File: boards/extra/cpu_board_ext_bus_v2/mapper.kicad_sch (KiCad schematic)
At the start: 3 parts, among them U2 74LS30, U7 74LS30, U8 ATF1502AS-7JX44

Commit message: Preparation for ordering with PCBWay.
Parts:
- U2, U7: MPN (none) -> 1-2199298-3; Manufacturer (none) -> TE Connectivity; Package (none) -> DIP-14
- U8: MPN (none) -> DS1032-44SDKT1A; Manufacturer (none) -> CONNFLY Elec; Package (none) -> Plugin-44P
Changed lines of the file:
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@@
       (effects (font (size 1.524 1.524)))
+    )
+    (property "Description" " 	44P PLCC Tin 1.27mm Plugin-44P IC / Transistor Socket ROHS " (at 182.245 66.675 0)
+      (effects (font (size 1.27 1.27)) hide)
+    )
+    (property "MPN" "DS1032-44SDKT1A" (at 182.245 66.675 0)
+      (effects (font (size 1.27 1.27)) hide)
+    )
+    (property "Manufacturer" " 	CONNFLY Elec " (at 182.245 66.675 0)
+      (effects (font (size 1.27 1.27)) hide)
+    )
+    (property "Package" " Plugin-44P" (at 182.245 66.675 0)
+      (effects (font (size 1.27 1.27)) hide)
     )
     (pin "3")
@@
       (effects (font (size 1.27 1.27)) hide)
     )
+    (property "Description" " 	Tin Phosphor bronze DIP-14 IC / Transistor Socket ROHS " (at 100.965 184.15 0)
+      (effects (font (size 1.27 1.27)) hide)
+    )
+    (property "MPN" "1-2199298-3" (at 100.965 184.15 0)
+      (effects (font (size 1.27 1.27)) hide)
+    )
+    (property "Manufacturer" "TE Connectivity " (at 100.965 184.15 0)
+      (effects (font (size 1.27 1.27)) hide)
+    )
+    (property "Package" "DIP-14" (at 100.965 184.15 0)
+      (effects (font (size 1.27 1.27)) hide)
+    )
     (pin "3")
     (pin "1")
@@
       (effects (font (size 1.27 1.27)) hide)
     )
+    (property "Description" " 	Tin Phosphor bronze DIP-14 IC / Transistor Socket ROHS " (at 116.205 54.61 0)
+      (effects (font (size 1.27 1.27)) hide)
+    )
+    (property "MPN" "1-2199298-3" (at 116.205 54.61 0)
+      (effects (font (size 1.27 1.27)) hide)
+    )
+    (property "Manufacturer" "TE Connectivity " (at 116.205 54.61 0)
+      (effects (font (size 1.27 1.27)) hide)
+    )
+    (property "Package" "DIP-14" (at 116.205 54.61 0)
+      (effects (font (size 1.27 1.27)) hide)
+    )

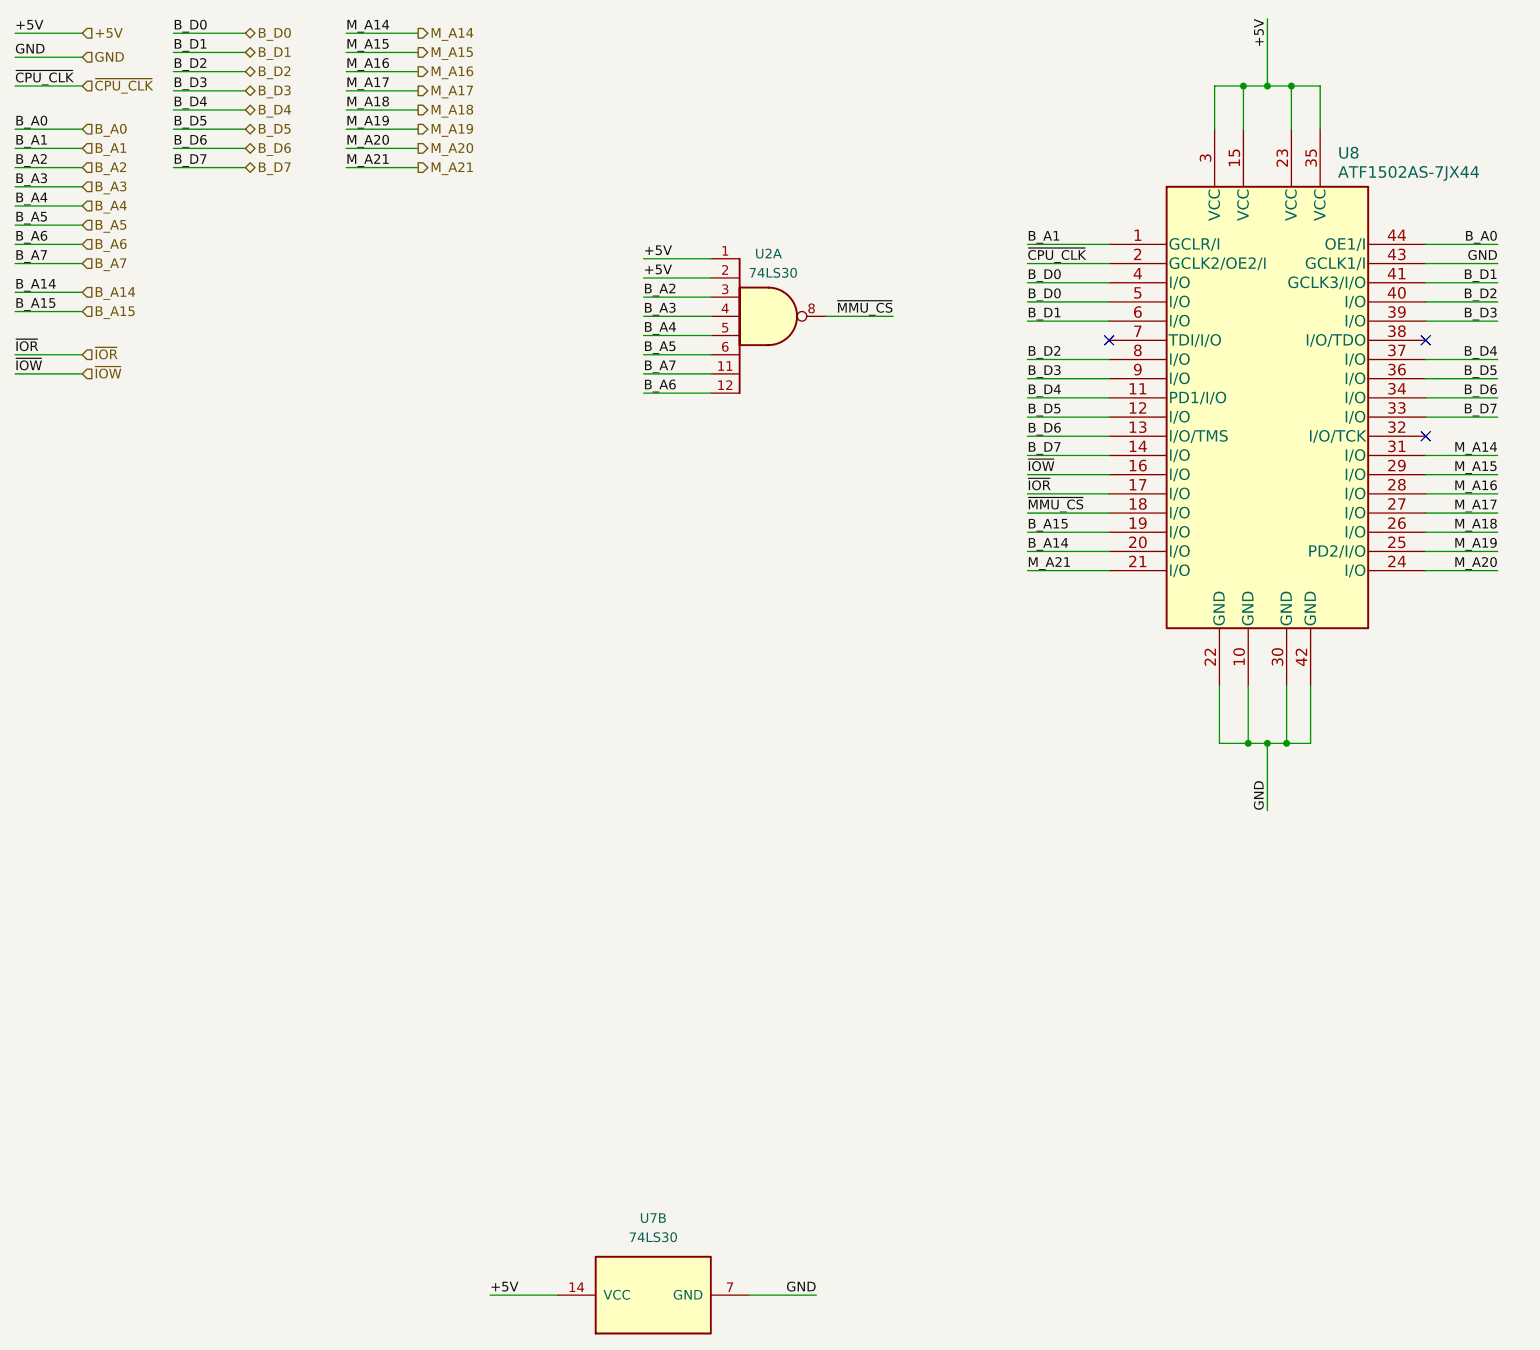
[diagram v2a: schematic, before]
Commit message: Upgraded board to KiCad 8 and imported design rules from the PCBWay website.
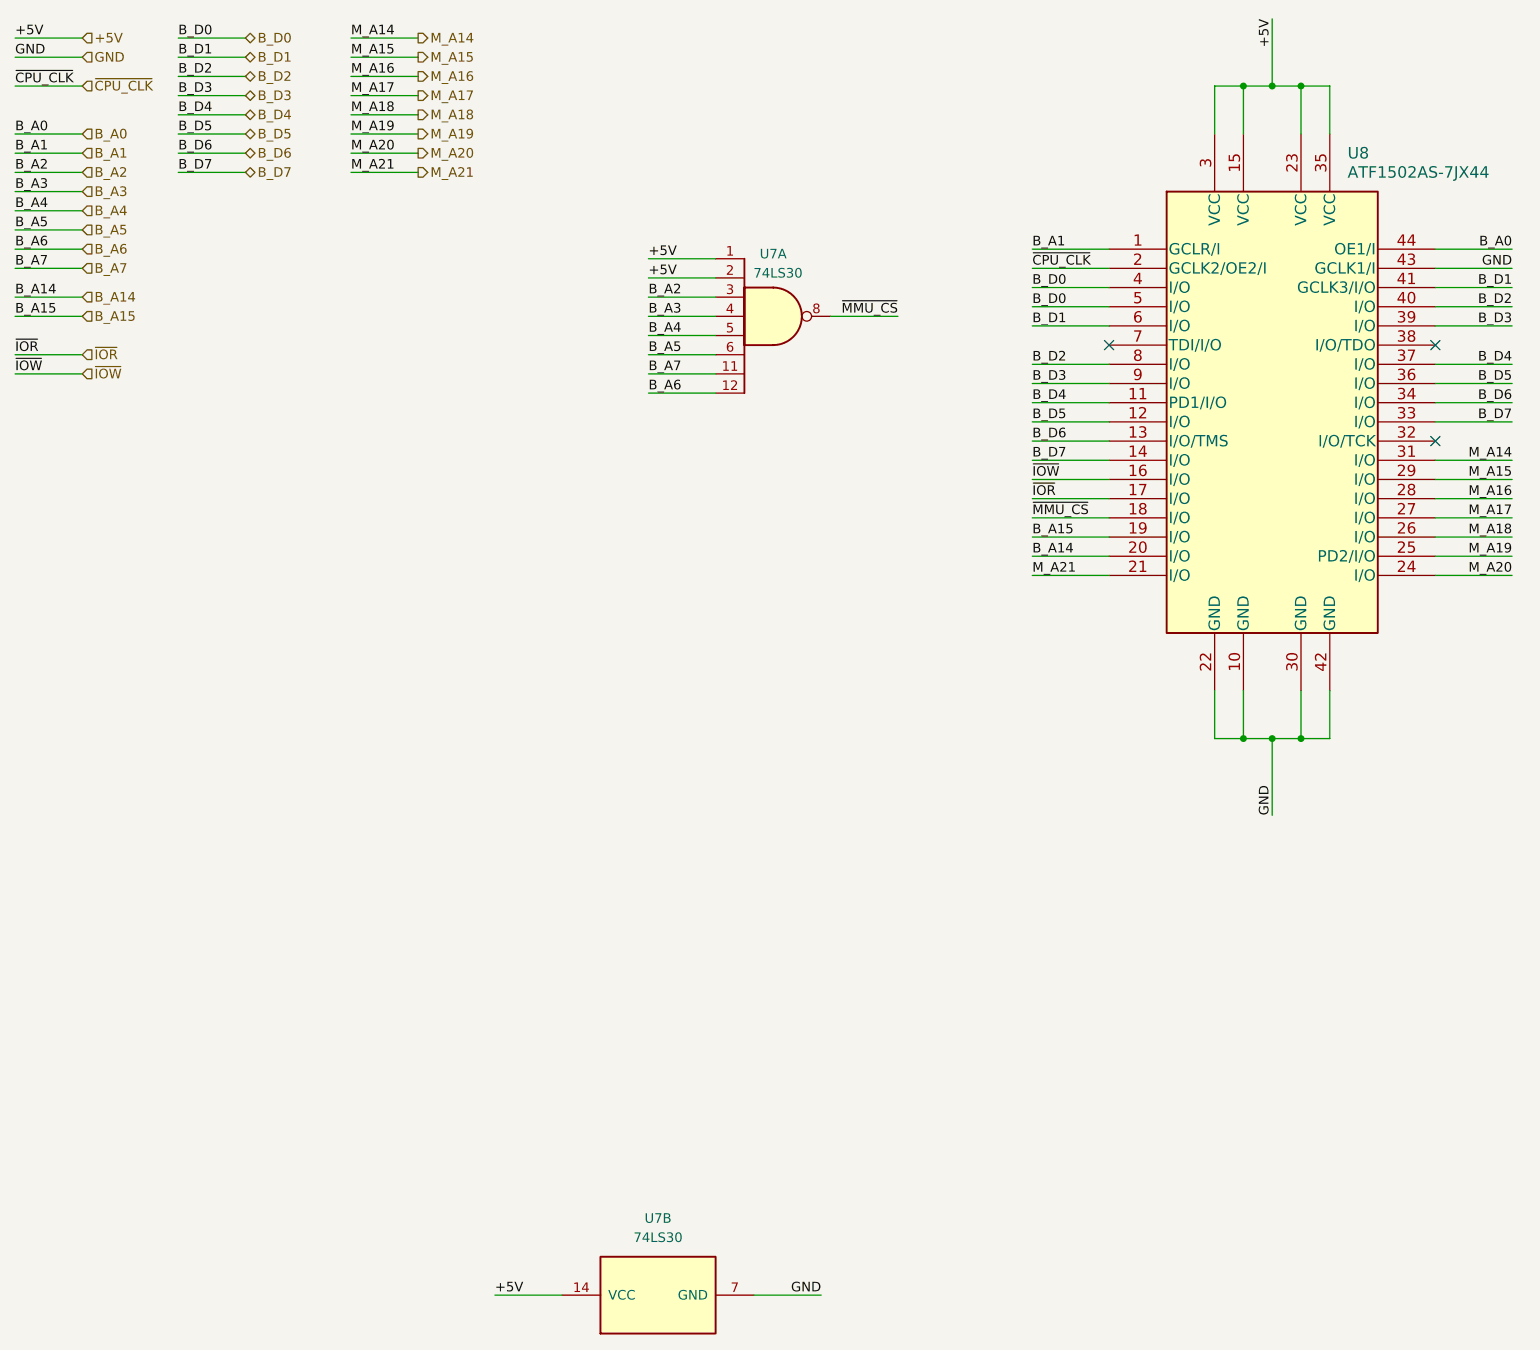
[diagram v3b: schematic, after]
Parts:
- renumbered U2 to U7
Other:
- moved on the sheet: U7A, U7B, U8
